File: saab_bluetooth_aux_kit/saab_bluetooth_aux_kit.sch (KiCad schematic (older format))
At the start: 4 parts, among them U1 CC3-0505SF-E, U2 ESP32-WROOM-DEVKIT, U3 MCP2515_MODULE, U4 UDA1334A_BREAKOUT

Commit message: Made simple PCB
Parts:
- added J?: Barrel_Jack, Connector_BarrelJack:BarrelJack_Wuerth_6941xx301002, symbol Connector:Barrel_Jack
- U2: value ESP32-WROOM-DEVKIT -> ESP32-WROOM-DEVKIT-custom_symbols
- U3: footprint (none) -> custom_footprints:MCP2515_Module
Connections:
- net 3VDC: no longer U4.DEEM
- net at U1.1 (+Vin): now also J?.1
- net at U1.3 (-Vin): now also J?.2
- no-connect marks 0 -> 2
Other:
- moved on the sheet: U2
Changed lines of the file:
@@
 L custom_symbols:ESP32-WROOM-DEVKIT U2
 U 1 1 5EA5CF06
-P 5100 4250
-F 0 "U2" H 5075 2982 118 0000 C CNN
-F 1 "ESP32-WROOM-DEVKIT" H 5075 3175 118 0000 C CNN
-F 2 "custom_footprints:ESP32-WROOM-30GPIO" H 5100 4250 118 0001 C CNN
-F 3 "" H 5100 4250 118 0001 C CNN
-	1    5100 4250
-	-1   0    0    1
+P 5100 4550
+F 0 "U2" H 5075 3282 118 0000 C CNN
+F 1 "ESP32-WROOM-DEVKIT-custom_symbols" H 5075 3475 118 0000 C CNN
+F 2 "custom_footprints:ESP32-WROOM-30GPIO" H 5100 4550 118 0001 C CNN
+F 3 "" H 5100 4550 118 0001 C CNN
+	1    5100 4550
+	1    0    0    -1
 $EndComp
 $Comp
@@
 F 0 "U3" V 6846 3272 50  0000 R CNN
 F 1 "MCP2515_MODULE" V 6755 3272 50  0000 R CNN
-F 2 "" H 6750 3750 50  0001 C CNN
+F 2 "custom_footprints:MCP2515_Module" H 6750 3750 50  0001 C CNN
 F 3 "" H 6750 3750 50  0001 C CNN
 	1    6800 3750
@@
 Text GLabel 3600 3700 2    50   Input ~ 10
 GND
-Text GLabel 5900 3800 2    50   Input ~ 10
+Text GLabel 4300 5000 0    50   Input ~ 10
 GND
-Text GLabel 5900 3700 2    50   Input ~ 10
+Text GLabel 4300 5100 0    50   Input ~ 10
 5VDC
 Text GLabel 7200 4150 3    50   Input ~ 10
@@
 Text GLabel 7100 4150 3    50   Input ~ 10
 GND
-Text GLabel 4350 3700 0    50   Input ~ 10
+Text GLabel 5850 5100 2    50   Input ~ 10
 3VDC
-Text GLabel 4350 3800 0    50   Input ~ 10
+Text GLabel 5850 5000 2    50   Input ~ 10
 GND
 Text GLabel 7000 4150 3    50   Input ~ 0
 SPI_CS
-Text GLabel 4350 4400 0    50   Input ~ 0
+Text GLabel 5850 4400 2    50   Input ~ 0
 SPI_CS
 Text GLabel 6700 4150 3    50   Input ~ 0
 SPI_SCLK
-Text GLabel 4350 4500 0    50   Input ~ 0
+Text GLabel 5850 4300 2    50   Input ~ 0
 SPI_SCLK
 Text GLabel 6900 4150 3    50   Input ~ 0
 SPI_MISO
-Text GLabel 4350 4600 0    50   Input ~ 0
+Text GLabel 5850 4200 2    50   Input ~ 0
 SPI_MISO
-Text GLabel 4350 5100 0    50   Input ~ 0
+Text GLabel 5850 3700 2    50   Input ~ 0
 SPI_MOSI
 Text GLabel 6800 4150 3    50   Input ~ 0
@@
 Text GLabel 7100 5950 3    50   Input ~ 0
 I2S_WSEL
-Text GLabel 5900 4400 2    50   Input ~ 0
+Text GLabel 4300 4400 0    50   Input ~ 0
 I2S_WSEL
 Text GLabel 7200 5950 3    50   Input ~ 0
 I2S_DIN
-Text GLabel 4350 5000 0    50   Input ~ 0
+Text GLabel 5850 3800 2    50   Input ~ 0
 I2S_DIN
 Text GLabel 7300 5950 3    50   Input ~ 0
 I2S_BCLK
-Text GLabel 5900 4300 2    50   Input ~ 0
+Text GLabel 4300 4500 0    50   Input ~ 0
 I2S_BCLK
 Text GLabel 7050 5050 1    50   Input ~ 10
@@
 Text GLabel 7250 5050 1    50   Input ~ 10
 GND
-Text GLabel 7450 5050 2    50   Input ~ 10
-3VDC
+NoConn ~ 6850 3350
+NoConn ~ 6950 3350
+$Comp
+L Connector:Barrel_Jack J?
+U 1 1 5EB35333
+P 1900 3700
+F 0 "J?" H 1957 4025 50  0000 C CNN
+F 1 "Barrel_Jack" H 1957 3934 50  0000 C CNN
+F 2 "Connector_BarrelJack:BarrelJack_Wuerth_6941xx301002" H 1950 3660 50  0001 C CNN
+F 3 "~" H 1950 3660 50  0001 C CNN
+	1    1900 3700
+	1    0    0    -1
+$EndComp
+Wire Wire Line
+	2200 3600 2600 3600
+Wire Wire Line
+	2600 3600 2600 3500
+Wire Wire Line
+	2200 3800 2300 3800
+Wire Wire Line
+	2300 3800 2300 3900
+Wire Wire Line
+	2300 3900 2600 3900
 $EndSCHEMATC

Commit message: Updated CAN connector pads
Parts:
- U1: value CC3-0505SF-E -> CC3-1205SF-E; symbol custom_symbols:CC3-0505SF-E -> custom_symbols:CC3-1205SF-E
- U2: value ESP32-WROOM-DEVKIT-custom_symbols -> ESP32-WROOM-30GPIO
- gave numbers to parts that had none: 1
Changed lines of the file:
@@
 P 5100 4550
 F 0 "U2" H 5075 3282 118 0000 C CNN
-F 1 "ESP32-WROOM-DEVKIT-custom_symbols" H 5075 3475 118 0000 C CNN
+F 1 "ESP32-WROOM-30GPIO" H 5075 3475 118 0000 C CNN
 F 2 "custom_footprints:ESP32-WROOM-30GPIO" H 5100 4550 118 0001 C CNN
 F 3 "" H 5100 4550 118 0001 C CNN
@@
 $EndComp
 $Comp
-L custom_symbols:CC3-0505SF-E U1
+L custom_symbols:CC3-1205SF-E U1
 U 1 1 5EA608C5
 P 3100 3700
 F 0 "U1" H 3100 4125 50  0000 C CNN
-F 1 "CC3-0505SF-E" H 3100 4034 50  0000 C CNN
+F 1 "CC3-1205SF-E" H 3100 4034 50  0000 C CNN
 F 2 "custom_footprints:CC3-1205SF-E" H 3100 3700 50  0001 C CNN
 F 3 "" H 3100 3700 50  0001 C CNN
@@
 NoConn ~ 6950 3350
 $Comp
-L Connector:Barrel_Jack J?
+L Connector:Barrel_Jack J1
 U 1 1 5EB35333
 P 1900 3700
-F 0 "J?" H 1957 4025 50  0000 C CNN
+F 0 "J1" H 1957 4025 50  0000 C CNN
 F 1 "Barrel_Jack" H 1957 3934 50  0000 C CNN
 F 2 "Connector_BarrelJack:BarrelJack_Wuerth_6941xx301002" H 1950 3660 50  0001 C CNN

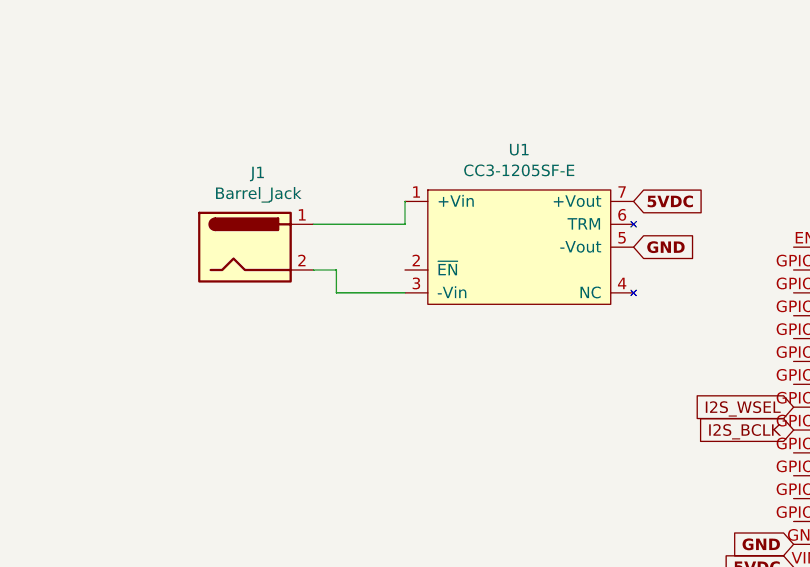
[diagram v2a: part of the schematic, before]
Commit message: Fixed CC3 DC-DC module footprint orientation. It was flipped. Tied enable pin to gnd. Re-routed I2C data.
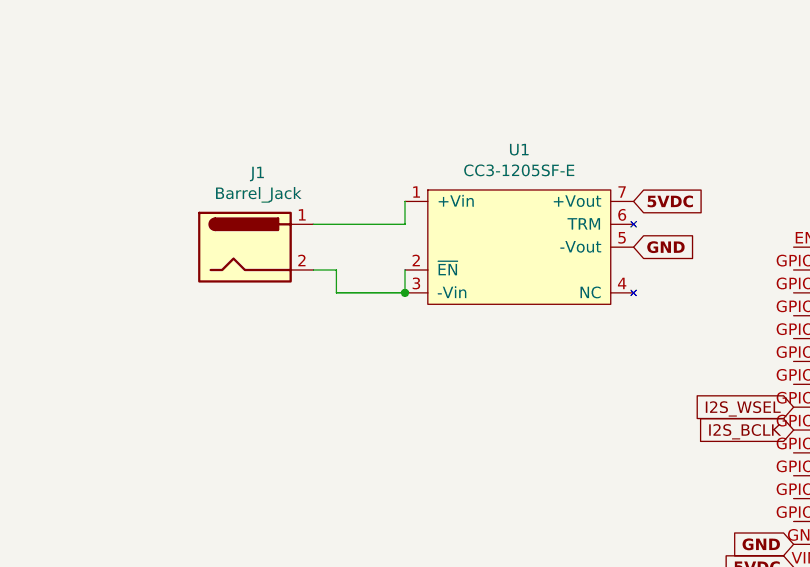
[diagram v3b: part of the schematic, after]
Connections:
- net at U1.2 (~EN): now also J1.2, U1.3 (-Vin)
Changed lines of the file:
@@
 Wire Wire Line
 	2300 3900 2600 3900
+Wire Wire Line
+	2600 3800 2600 3900
+Connection ~ 2600 3900
 $EndSCHEMATC
